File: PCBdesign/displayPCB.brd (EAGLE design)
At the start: 76.5 x 66.4 mm, 8 parts

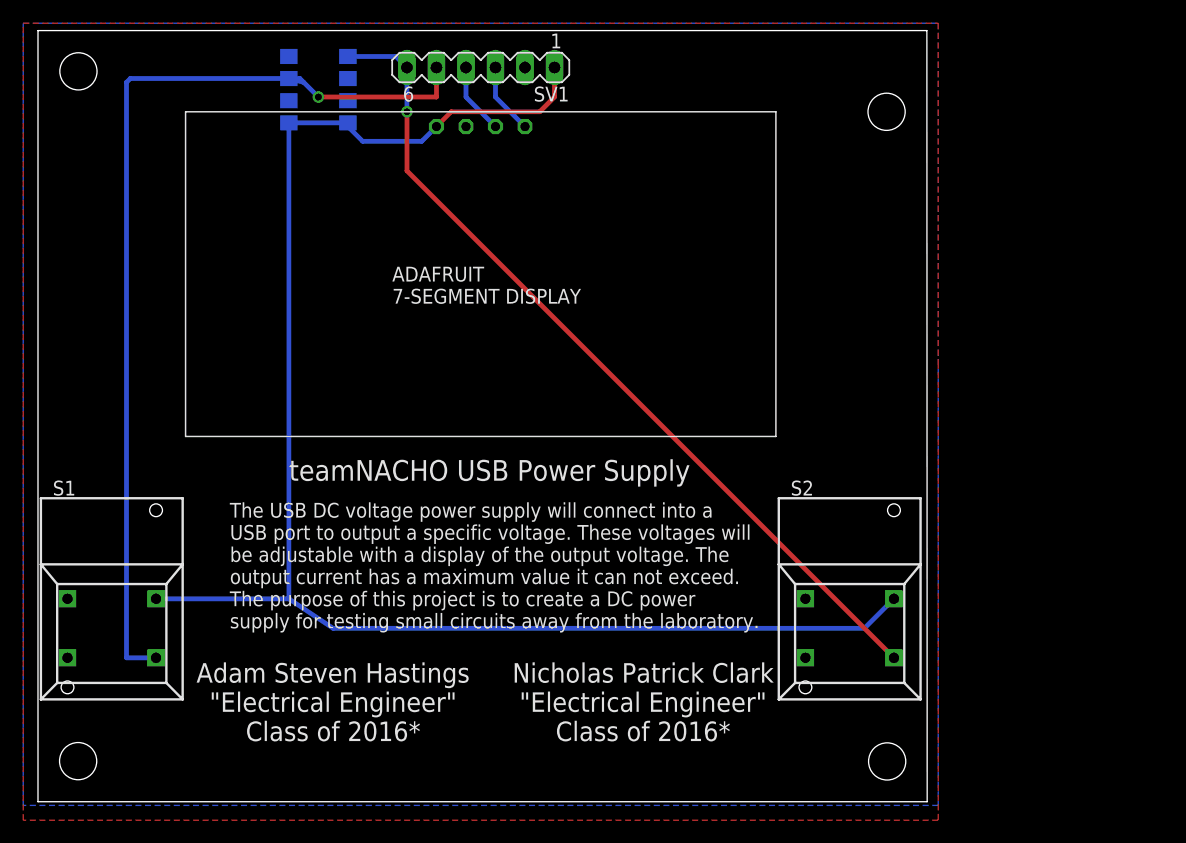
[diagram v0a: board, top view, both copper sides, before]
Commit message: trying to get font to fit
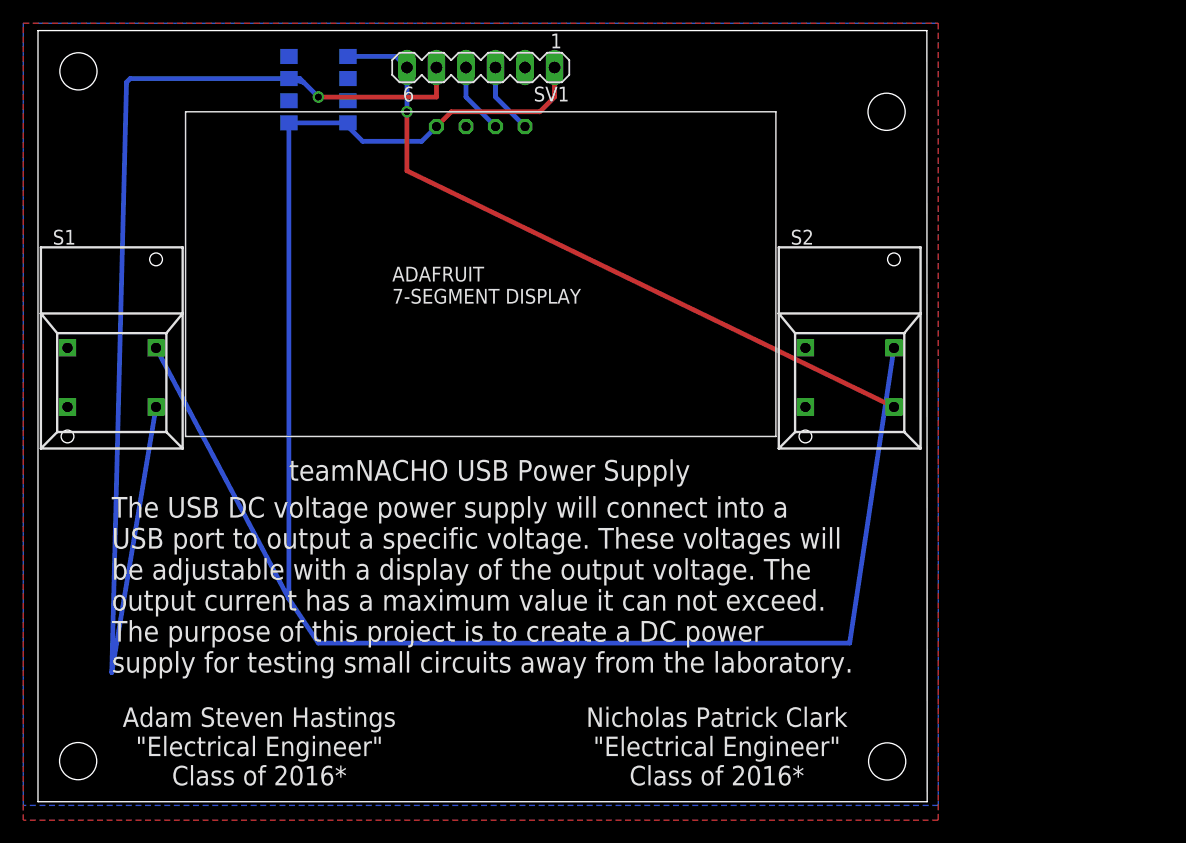
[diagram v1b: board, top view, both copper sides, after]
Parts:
- moved S1 21.6 mm to (6.35, 54.6)
- moved S2 21.6 mm to (69.8, 54.6)
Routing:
- net +5V: track 134.1 -> 169.2 mm
- net N$5: track 83.4 -> 105.3 mm
- net N$6: track 73.6 -> 60.9 mm
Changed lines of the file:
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@@
 <hole x="73.025" y="74.93" drill="3.2"/>
 <hole x="73.0758" y="19.0246" drill="3.2"/>
-<text x="16.51" y="30.48" size="1.27" layer="21">The USB DC voltage power supply will connect into a
+<text x="6.35" y="26.67" size="1.778" layer="21">The USB DC voltage power supply will connect into a
 USB port to output a specific voltage. These voltages will
 be adjustable with a display of the output voltage. The
@@
 supply for testing small circuits away from the laboratory.</text>
 <text x="21.59" y="43.18" size="1.778" layer="21">teamNACHO USB Power Supply</text>
-<text x="25.4" y="24.13" size="1.6764" layer="21" align="center">Adam Steven Hastings
+<text x="19.05" y="20.32" size="1.6764" layer="21" align="center">Adam Steven Hastings
 "Electrical Engineer"
 Class of 2016*</text>
-<text x="52.07" y="24.13" size="1.6764" layer="21" align="center">Nicholas Patrick Clark
+<text x="58.42" y="20.32" size="1.6764" layer="21" align="center">Nicholas Patrick Clark
 "Electrical Engineer"
 Class of 2016*</text>
 <text x="39.37" y="17.78" size="1.6764" layer="22" rot="MR0" align="center">*Dates may change due to unforseen circumstances</text>
-<text x="63.5" y="39.37" size="1.6764" layer="22" rot="MR0">Inputs and Outputs:
+<text x="72.39" y="38.1" size="1.6764" layer="22" rot="MR0">Inputs and Outputs:
 IN - DC voltage from the USB port.
 IN - User determined voltage setting.
@@
 <attribute name="NAME" x="29.21" y="79.375" size="1.27" layer="26" rot="MR270"/>
 </element>
-<element name="S1" library="switch" package="5501" value="5501" x="6.35" y="33.02" rot="R270"/>
-<element name="S2" library="switch" package="5501" value="5501" x="69.85" y="33.02" rot="R270"/>
+<element name="S1" library="switch" package="5501" value="5501" x="6.35" y="54.61" rot="R270"/>
+<element name="S2" library="switch" package="5501" value="5501" x="69.85" y="54.61" rot="R270"/>
 <element name="SV1" library="con-lstb" package="MA06-1" value="" x="38.1" y="78.74" rot="R180">
 <attribute name="OC_NEWARK" value="unknown" x="38.1" y="78.74" size="1.778" layer="27" rot="R180" display="off"/>
@@
 <contactref element="S1" pad="NO"/>
 <contactref element="R1" pad="1"/>
-<wire x1="10.16" y1="27.94" x2="7.62" y2="27.94" width="0.4064" layer="16"/>
-<wire x1="7.62" y1="27.94" x2="7.62" y2="77.47" width="0.4064" layer="16"/>
+<wire x1="10.16" y1="49.53" x2="6.35" y2="26.67" width="0.4064" layer="16"/>
+<wire x1="6.35" y1="26.67" x2="7.62" y2="77.47" width="0.4064" layer="16"/>
 <wire x1="22.86" y1="77.47" x2="21.59" y2="77.79" width="0.4064" layer="16"/>
 <wire x1="34.29" y1="78.74" x2="34.29" y2="76.2" width="0.4064" layer="1"/>
@@
 <wire x1="31.75" y1="78.74" x2="30.8" y2="79.69" width="0.4064" layer="16"/>
 <wire x1="30.8" y1="79.69" x2="26.67" y2="79.69" width="0.4064" layer="16"/>
-<wire x1="73.66" y1="27.94" x2="31.75" y2="69.85" width="0.4064" layer="1"/>
+<wire x1="73.66" y1="49.53" x2="31.75" y2="69.85" width="0.4064" layer="1"/>
 <wire x1="31.75" y1="69.85" x2="31.75" y2="74.93" width="0.4064" layer="1"/>
 <via x="31.75" y="74.93" extent="1-16" drill="0.6" shape="square"/>
@@
 <contactref element="S1" pad="1A"/>
 <contactref element="S2" pad="1A"/>
-<wire x1="10.16" y1="33.02" x2="21.59" y2="33.02" width="0.4064" layer="16"/>
+<wire x1="10.16" y1="54.61" x2="21.59" y2="33.02" width="0.4064" layer="16"/>
 <wire x1="21.59" y1="33.02" x2="21.59" y2="73.98" width="0.4064" layer="16"/>
 <wire x1="21.59" y1="73.98" x2="26.67" y2="73.98" width="0.4064" layer="16"/>
@@
 <wire x1="27.94" y1="72.39" x2="26.67" y2="73.66" width="0.4064" layer="16"/>
 <wire x1="26.67" y1="73.66" x2="26.67" y2="73.98" width="0.4064" layer="16"/>
-<wire x1="73.66" y1="33.02" x2="71.12" y2="30.48" width="0.4064" layer="16"/>
-<wire x1="71.12" y1="30.48" x2="25.4" y2="30.48" width="0.4064" layer="16"/>
-<wire x1="25.4" y1="30.48" x2="21.59" y2="33.02" width="0.4064" layer="16"/>
+<wire x1="73.66" y1="54.61" x2="69.85" y2="29.21" width="0.4064" layer="16"/>
+<wire x1="69.85" y1="29.21" x2="24.13" y2="29.21" width="0.4064" layer="16"/>
+<wire x1="24.13" y1="29.21" x2="21.59" y2="33.02" width="0.4064" layer="16"/>
 </signal>
 </signals>

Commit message: designPCB complete
PCB complete and uploaded to OSHpark for ordering
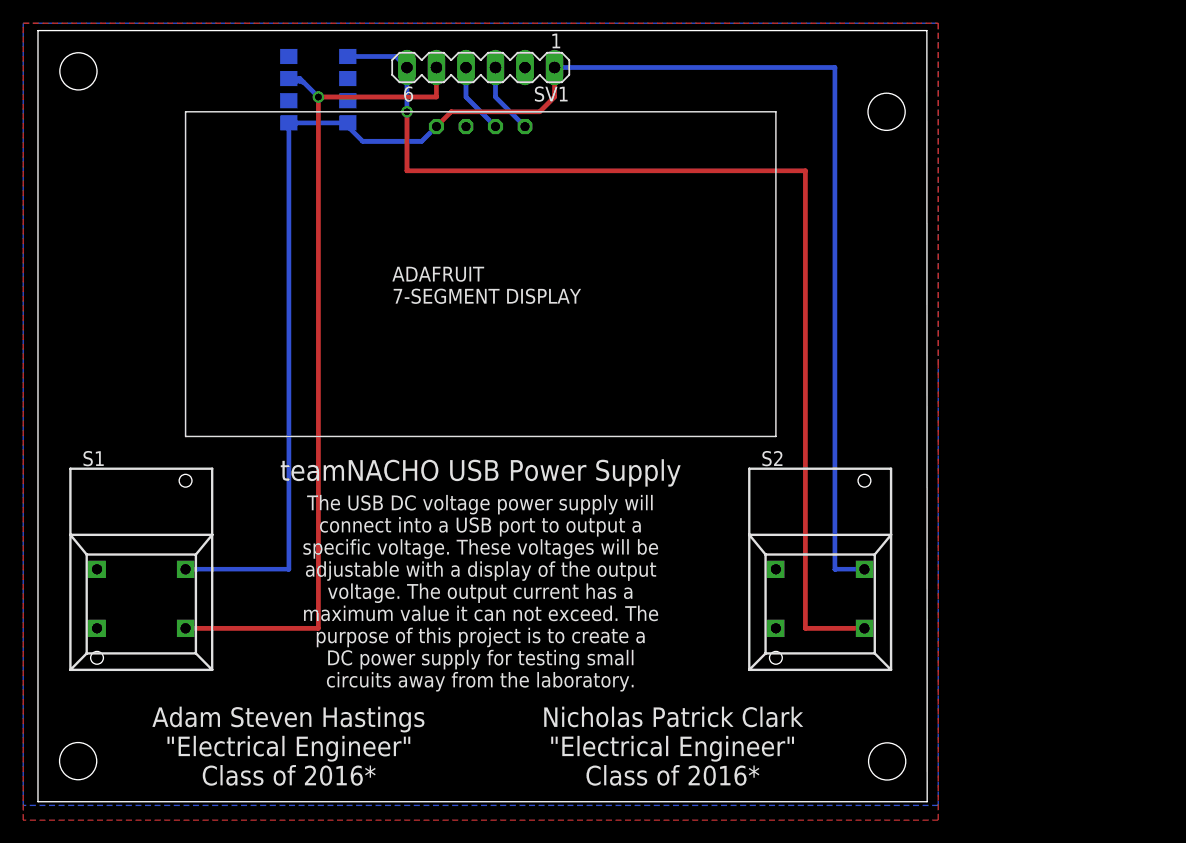
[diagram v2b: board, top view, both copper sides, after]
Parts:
- moved S1 19.2 mm to (8.89, 35.6)
- moved S2 19.2 mm to (67.3, 35.6)
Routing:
- net N$6: track 60.9 -> 93.1 mm
- net N$5: track 105.3 -> 74.4 mm
- net +5V: track 169.2 -> 144.7 mm
